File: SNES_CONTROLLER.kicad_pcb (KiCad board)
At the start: 2 copper layers, 57 x 76 mm, 24 parts, among them J2 Screw_Terminal_01x12, J3 Screw_Terminal_01x12, J4 Screw_Terminal_01x05, U1 4021, U2 4021

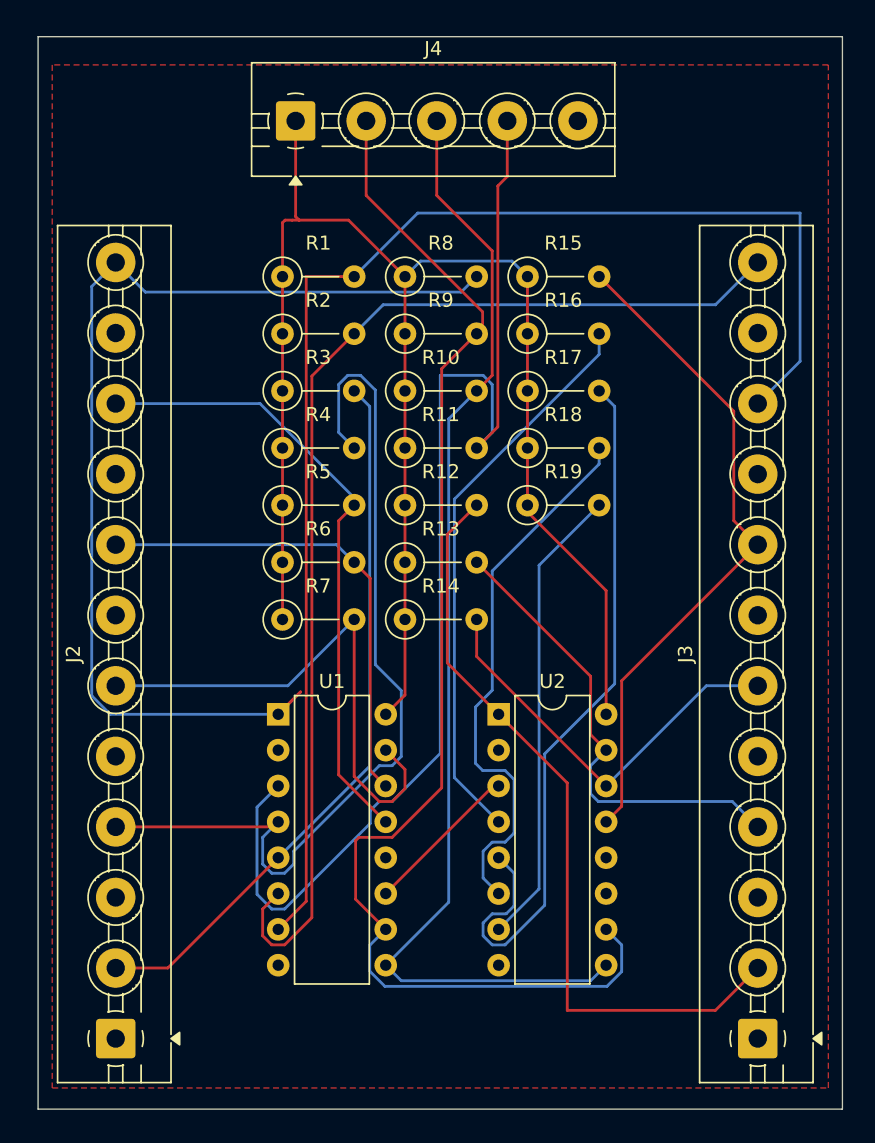
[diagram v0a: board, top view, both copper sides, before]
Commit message: changes reverted. Connector changed by a 6 pin one. Rounded PCB
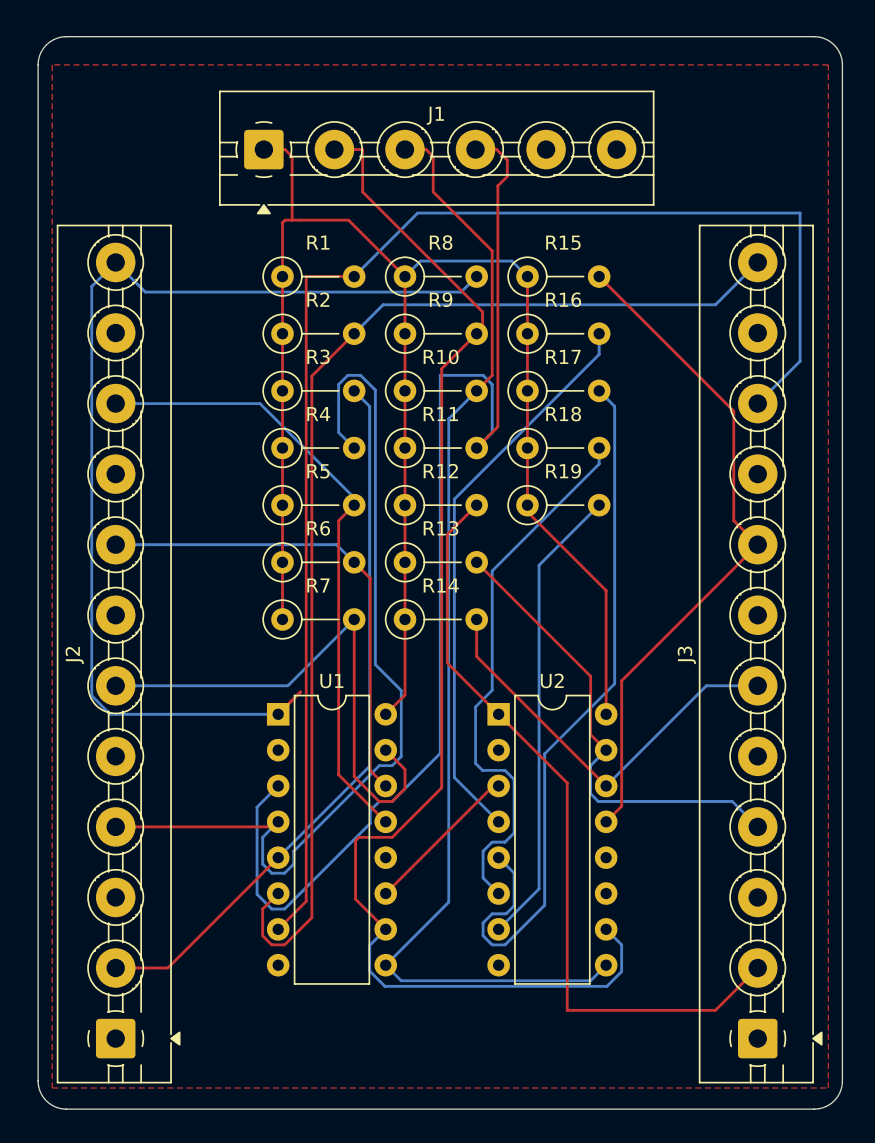
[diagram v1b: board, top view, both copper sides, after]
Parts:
- removed J4: Screw_Terminal_01x05, TerminalBlock:TerminalBlock_MaiXu_MX126-5.0-05P_1x05_P5.00mm
- added J1: Screw_Terminal_01x06, TerminalBlock:TerminalBlock_MaiXu_MX126-5.0-06P_1x06_P5.00mm, F.Cu at (114.0, 66.5)
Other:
- outline, holes or cut-outs redrawn

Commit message: Add silkscreens and M4 mount holes
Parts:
- added H1: MountingHole, MountingHole:MountingHole_4.3mm_M4, F.Cu at (127.0, 130.0)
- added H2: MountingHole, MountingHole:MountingHole_4.3mm_M4, F.Cu at (104.0, 65.5)
- added H3: MountingHole, MountingHole:MountingHole_4.3mm_M4, F.Cu at (149.0, 65.5)
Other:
- board text added: "SNES & Uzebox controller PCB v1.4"
- board text removed: "SNES & Uzebox controller PCB v1.0"

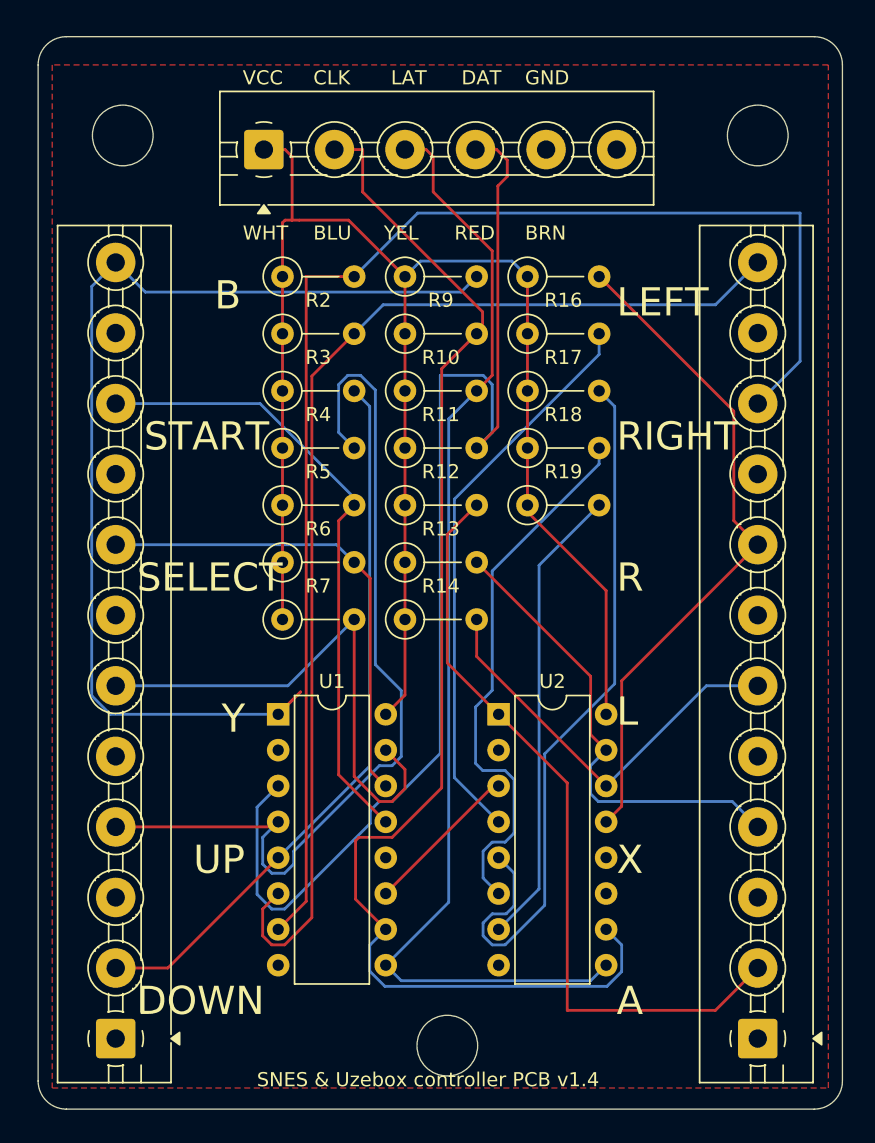
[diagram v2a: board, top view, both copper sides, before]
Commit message: Refactor schematic and board
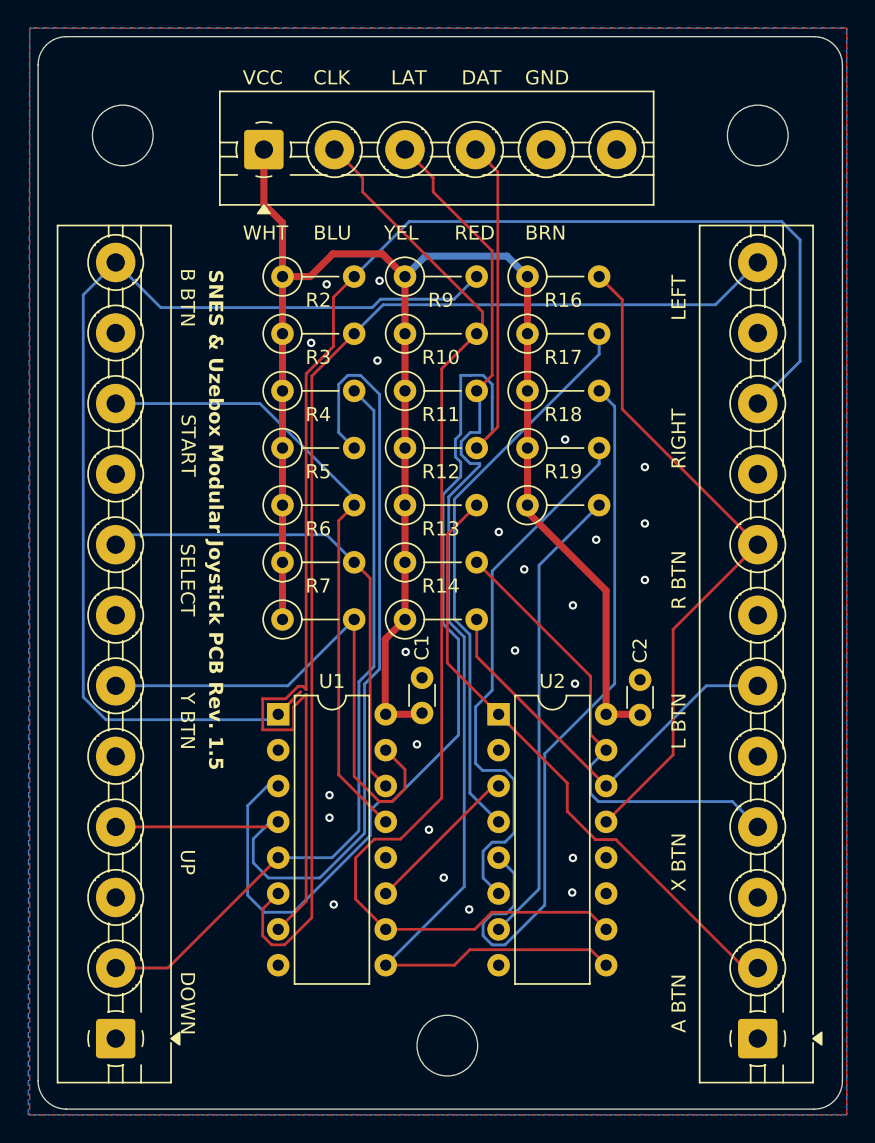
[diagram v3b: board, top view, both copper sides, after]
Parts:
- added C1: 0.01uf, Capacitor_THT:C_Disc_D3.0mm_W1.6mm_P2.50mm, F.Cu at (125.2, 106.4)
- added C2: 0.01uf, Capacitor_THT:C_Disc_D3.0mm_W1.6mm_P2.50mm, F.Cu at (140.7, 106.6)
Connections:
- J1 pad 6: unconnected-(J1-Pin_6-Pad6) -> /Gnd
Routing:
- net Net-(J3-Pin_2): track 54.9 -> 44.2 mm
- net /Clk: track 92.4 -> 81.9 mm
- net Net-(J3-Pin_10): track 98.7 -> 105.6 mm
- net /Vcc: track 119.7 -> 123.7 mm
- net Net-(J2-Pin_2): track 51.0 -> 53.5 mm
- net Net-(J2-Pin_12): track 76.6 -> 78.7 mm
- net /Latch: track 80.9 -> 83.0 mm
- net Net-(J2-Pin_4): track 64.2 -> 65.5 mm
- net /Data1: track 86.4 -> 87.4 mm
- net Net-(J2-Pin_8): track 34.2 -> 34.8 mm
- net /Gnd: vias 0 -> 24
- added copper zone on B.Cu, net /Gnd
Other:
- board text added: "${TITLE} Rev. ${REVISION}"
- board text added: "A BTN"
- board text added: "B BTN"
- board text added: "L BTN"
- board text added: "R BTN"
- board text added: "X BTN"
- board text added: "Y BTN"
- board text removed: "A"
- board text removed: "B"
- board text removed: "L"
- board text removed: "R"
- board text removed: "SNES & Uzebox controller PCB v1.4"
- board text removed: "X"
- board text removed: "Y"
